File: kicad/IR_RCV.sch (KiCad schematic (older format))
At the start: 19 parts, among them P10 Partition, P5 PR_Host, P6 PR_Slave, P7 Partition, P8 Partition, P9 Partition, Q1 DMN3065LW-7, U6 AD8601

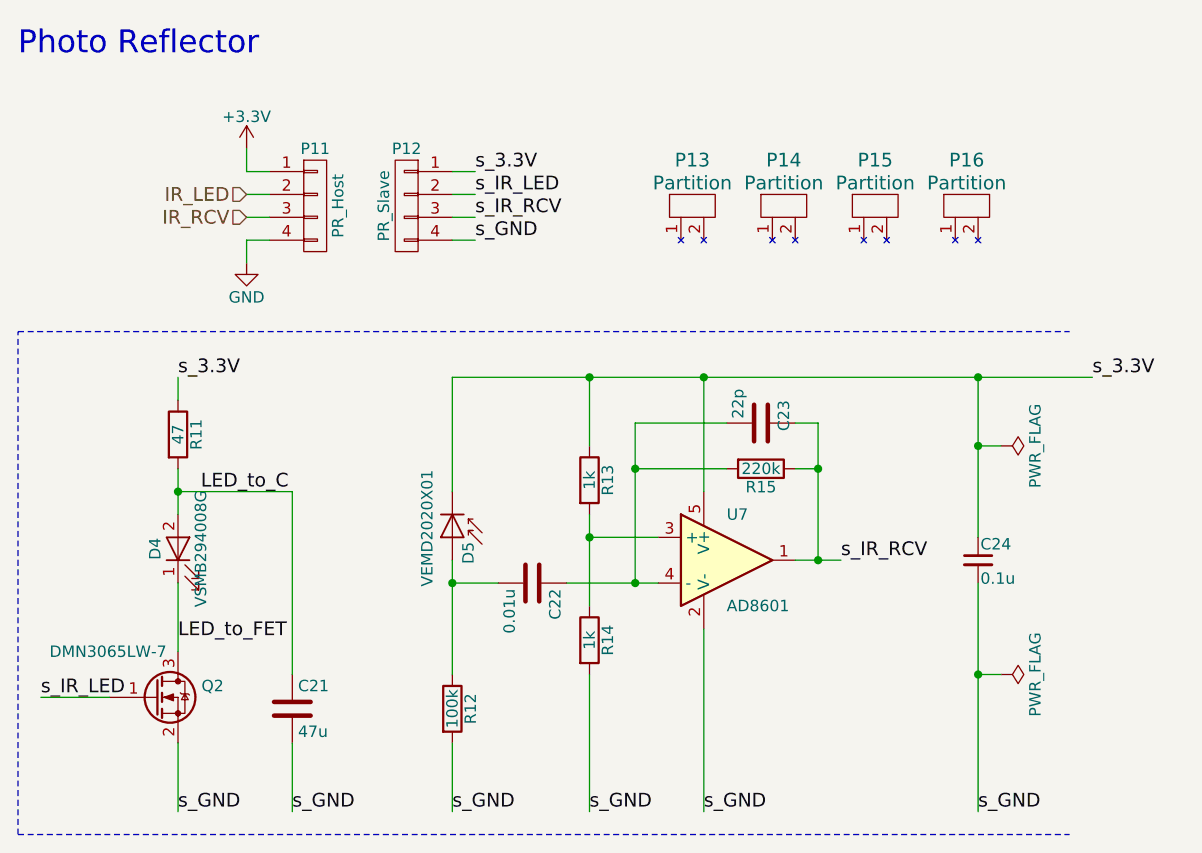
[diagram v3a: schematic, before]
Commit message: フットプリントを改良，アナログ電源を分離
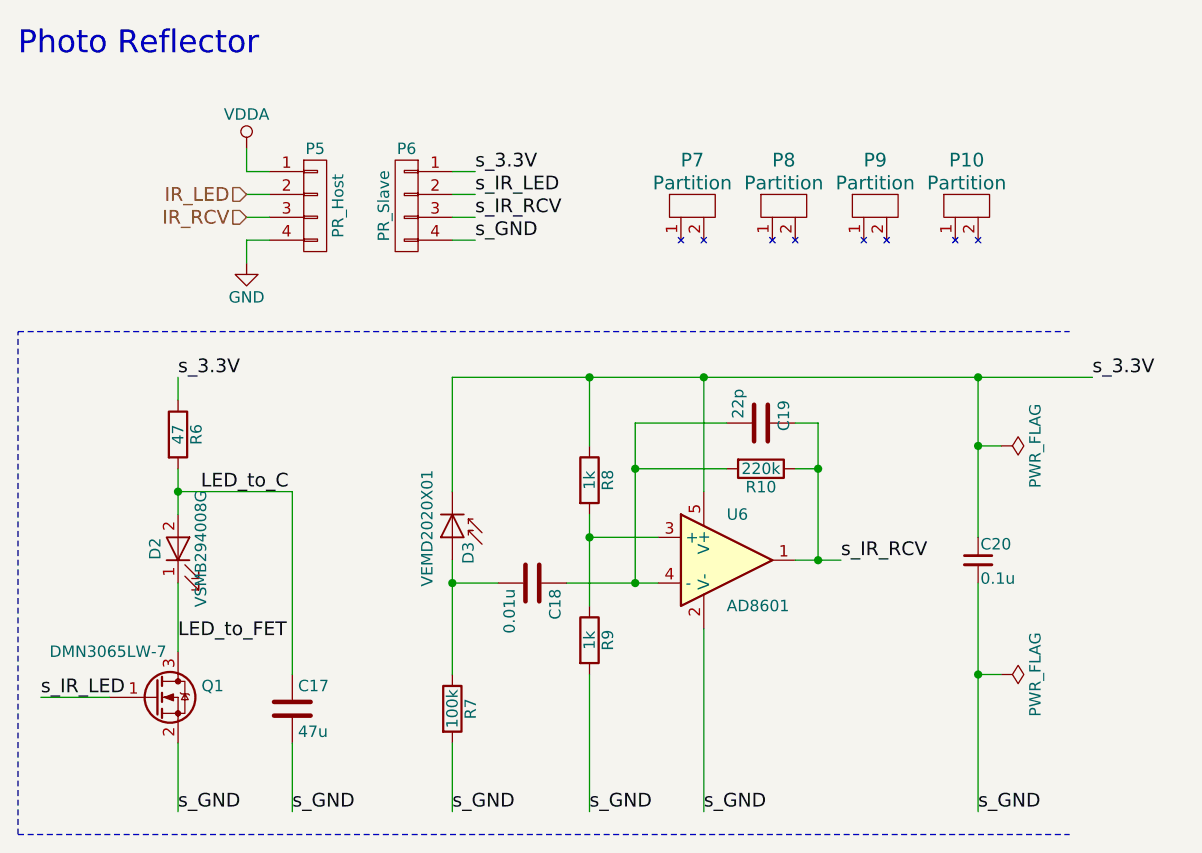
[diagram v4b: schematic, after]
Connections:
- net +3V3 renamed VDDA
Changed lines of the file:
@@
 AR Path="/597E1B35/589BE652" Ref="P25"  Part="1"
 AR Path="/597E1B39/589BE652" Ref="P31"  Part="1"
-F 0 "P12" H 5400 2800 50  0000 C CNN
+F 0 "P6" H 5400 2800 50  0000 C CNN
 F 1 "PR_Slave" V 5500 2550 50  0000 C CNN
 F 2 "mouse:STAND_PR_SLAVE" H 5400 2550 50  0001 C CNN
@@
 AR Path="/597E1B35/589BE75A" Ref="Q5"  Part="1"
 AR Path="/597E1B39/589BE75A" Ref="Q6"  Part="1"
-F 0 "Q2" H 4600 4750 50  0000 R CNN
+F 0 "Q1" H 4600 4750 50  0000 R CNN
 F 1 "DMN3065LW-7" H 4350 4900 50  0000 R CNN
 F 2 "TO_SOT_Packages_SMD:SOT-323_SC-70" H 4500 4800 50  0001 C CNN
@@
 AR Path="/597E1B35/589BE76D" Ref="R24"  Part="1"
 AR Path="/597E1B39/589BE76D" Ref="R29"  Part="1"
-F 0 "R11" V 4480 3550 50  0000 C CNN
+F 0 "R6" V 4480 3550 50  0000 C CNN
 F 1 "47" V 4400 3550 50  0000 C CNN
 F 2 "Resistors_SMD:R_0603" V 4330 3550 50  0001 C CNN
@@
 AR Path="/597E1B35/589BE88F" Ref="P24"  Part="1"
 AR Path="/597E1B39/589BE88F" Ref="P30"  Part="1"
-F 0 "P11" H 5000 2800 50  0000 C CNN
+F 0 "P5" H 5000 2800 50  0000 C CNN
 F 1 "PR_Host" V 5100 2550 50  0000 C CNN
 F 2 "mouse:STAND_PR_HOST" H 5000 2550 50  0001 C CNN
@@
 AR Path="/597E1B35/589BEE3B" Ref="R25"  Part="1"
 AR Path="/597E1B39/589BEE3B" Ref="R30"  Part="1"
-F 0 "R12" V 5680 4750 50  0000 C CNN
+F 0 "R7" V 5680 4750 50  0000 C CNN
 F 1 "100k" V 5600 4750 50  0000 C CNN
 F 2 "Resistors_SMD:R_0201" V 5530 4750 50  0001 C CNN
@@
 AR Path="/597E1B35/589BF265" Ref="#PWR074"  Part="1"
 AR Path="/597E1B39/589BF265" Ref="#PWR078"  Part="1"
-F 0 "#PWR078" H 4700 2550 50  0001 C CNN
+F 0 "#PWR038" H 4700 2550 50  0001 C CNN
 F 1 "GND" H 4700 2650 50  0000 C CNN
 F 2 "" H 4700 2800 50  0000 C CNN
@@
 AR Path="/597E1B35/589EE263" Ref="C32"  Part="1"
 AR Path="/597E1B39/589EE263" Ref="C36"  Part="1"
-F 0 "C21" H 4925 4850 50  0000 L CNN
+F 0 "C17" H 4925 4850 50  0000 L CNN
 F 1 "47u" H 4925 4650 50  0000 L CNN
 F 2 "Capacitors_SMD:C_0805" H 4938 4600 50  0001 C CNN
@@
 Text Label 4500 3800 0    60   ~ 0
 LED_to_C
-$Comp
-L +3.3V #PWR039
-U 1 1 589CC209
-P 4700 2300
-AR Path="/57CF0B09/589CC209" Ref="#PWR039"  Part="1"
-AR Path="/57CF2A30/589CC209" Ref="#PWR043"  Part="1"
-AR Path="/597E1B35/589CC209" Ref="#PWR075"  Part="1"
-AR Path="/597E1B39/589CC209" Ref="#PWR079"  Part="1"
-F 0 "#PWR079" H 4700 2150 50  0001 C CNN
-F 1 "+3.3V" H 4700 2440 50  0000 C CNN
-F 2 "" H 4700 2300 50  0000 C CNN
-F 3 "" H 4700 2300 50  0000 C CNN
-	1    4700 2300
-	1    0    0    -1
-$EndComp
 Text Label 7300 4100 0    60   ~ 0
 s_IR_RCV
@@
 AR Path="/597E1B35/58A0483E" Ref="R26"  Part="1"
 AR Path="/597E1B39/58A0483E" Ref="R31"  Part="1"
-F 0 "R13" V 6280 3750 50  0000 C CNN
+F 0 "R8" V 6280 3750 50  0000 C CNN
 F 1 "1k" V 6200 3750 50  0000 C CNN
 F 2 "Resistors_SMD:R_0201" V 6130 3750 50  0001 C CNN
@@
 AR Path="/597E1B35/57CF0F5E" Ref="C34"  Part="1"
 AR Path="/597E1B39/57CF0F5E" Ref="C38"  Part="1"
-F 0 "C23" H 6850 3600 50  0000 L CNN
+F 0 "C19" H 6850 3600 50  0000 L CNN
 F 1 "22p" H 6800 3400 50  0000 L CNN
 F 2 "Capacitors_SMD:C_0201" H 6988 3350 50  0001 C CNN
@@
 AR Path="/597E1B35/57CF0F57" Ref="R28"  Part="1"
 AR Path="/597E1B39/57CF0F57" Ref="R33"  Part="1"
-F 0 "R15" V 7030 3700 50  0000 C CNN
+F 0 "R10" V 7030 3700 50  0000 C CNN
 F 1 "220k" V 6950 3700 50  0000 C CNN
 F 2 "Resistors_SMD:R_0201" V 6880 3700 50  0001 C CNN
@@
 AR Path="/597E1B35/5925867D" Ref="C35"  Part="1"
 AR Path="/597E1B39/5925867D" Ref="C39"  Part="1"
-F 0 "C24" H 7910 4170 50  0000 L CNN
+F 0 "C20" H 7910 4170 50  0000 L CNN
 F 1 "0.1u" H 7910 4020 50  0000 L CNN
 F 2 "Capacitors_SMD:C_0201" H 7900 4100 50  0001 C CNN
@@
 AR Path="/597E1B35/58A04889" Ref="R27"  Part="1"
 AR Path="/597E1B39/58A04889" Ref="R32"  Part="1"
-F 0 "R14" V 6280 4450 50  0000 C CNN
+F 0 "R9" V 6280 4450 50  0000 C CNN
 F 1 "1k" V 6200 4450 50  0000 C CNN
 F 2 "Resistors_SMD:R_0201" V 6130 4450 50  0001 C CNN
@@
 AR Path="/597E1B35/57CF0F45" Ref="C33"  Part="1"
 AR Path="/597E1B39/57CF0F45" Ref="C37"  Part="1"
-F 0 "C22" H 5975 4300 50  0000 L CNN
+F 0 "C18" H 5975 4300 50  0000 L CNN
 F 1 "0.01u" H 5975 4100 50  0000 L CNN
 F 2 "Capacitors_SMD:C_0201" H 5988 4050 50  0001 C CNN
@@
 AR Path="/597E1B35/59497B18" Ref="P26"  Part="1"
 AR Path="/597E1B39/59497B18" Ref="P32"  Part="1"
-F 0 "P13" H 6650 2550 60  0000 C CNN
+F 0 "P7" H 6650 2550 60  0000 C CNN
 F 1 "Partition" H 6650 2450 60  0000 C CNN
 F 2 "mouse:Partition_Host" H 6650 2450 60  0001 C CNN
@@
 AR Path="/597E1B35/59497CA2" Ref="P27"  Part="1"
 AR Path="/597E1B39/59497CA2" Ref="P33"  Part="1"
-F 0 "P14" H 7050 2550 60  0000 C CNN
+F 0 "P8" H 7050 2550 60  0000 C CNN
 F 1 "Partition" H 7050 2450 60  0000 C CNN
 F 2 "mouse:Partition_Slave" H 7050 2450 60  0001 C CNN
@@
 AR Path="/597E1B35/59497CF1" Ref="P28"  Part="1"
 AR Path="/597E1B39/59497CF1" Ref="P34"  Part="1"
-F 0 "P15" H 7450 2550 60  0000 C CNN
+F 0 "P9" H 7450 2550 60  0000 C CNN
 F 1 "Partition" H 7450 2450 60  0000 C CNN
 F 2 "mouse:Partition_Long_Host" H 7450 2450 60  0001 C CNN
@@
 AR Path="/597E1B35/59497D43" Ref="P29"  Part="1"
 AR Path="/597E1B39/59497D43" Ref="P35"  Part="1"
-F 0 "P16" H 7850 2550 60  0000 C CNN
+F 0 "P10" H 7850 2550 60  0000 C CNN
 F 1 "Partition" H 7850 2450 60  0000 C CNN
 F 2 "mouse:Partition_long_Slave" H 7850 2450 60  0001 C CNN
@@
 AR Path="/597E1B35/594AC13D" Ref="U12"  Part="1"
 AR Path="/597E1B39/594AC13D" Ref="U13"  Part="1"
-F 0 "U7" H 6800 4300 50  0000 L CNN
+F 0 "U6" H 6800 4300 50  0000 L CNN
 F 1 "AD8601" H 6800 3900 50  0000 L CNN
 F 2 "TO_SOT_Packages_SMD:SOT-23-5" H 6800 3700 50  0001 C CNN
@@
 AR Path="/597E1B35/594AC36C" Ref="D11"  Part="1"
 AR Path="/597E1B39/594AC36C" Ref="D13"  Part="1"
-F 0 "D5" H 5620 4070 50  0000 L CNN
+F 0 "D3" H 5620 4070 50  0000 L CNN
 F 1 "VEMD2020X01" H 5560 3890 50  0000 C CNN
 F 2 "mouse:VISHAY_DIODE" H 5550 4000 50  0001 C CNN
@@
 AR Path="/597E1B35/594AC674" Ref="D10"  Part="1"
 AR Path="/597E1B39/594AC674" Ref="D12"  Part="1"
-F 0 "D4" H 4400 4150 50  0000 C CNN
+F 0 "D2" H 4400 4150 50  0000 C CNN
 F 1 "VSMB294008G" H 4400 3950 50  0000 C CNN
 F 2 "mouse:VISHAY_DIODE" H 4400 4050 50  0001 C CNN
@@
 AR Path="/597E1B35/594B7401" Ref="#FLG076"  Part="1"
 AR Path="/597E1B39/594B7401" Ref="#FLG080"  Part="1"
-F 0 "#FLG080" H 8000 3675 50  0001 C CNN
+F 0 "#FLG040" H 8000 3675 50  0001 C CNN
 F 1 "PWR_FLAG" H 8000 3750 50  0000 C CNN
 F 2 "" H 8000 3600 50  0001 C CNN
@@
 AR Path="/597E1B35/594B744C" Ref="#FLG077"  Part="1"
 AR Path="/597E1B39/594B744C" Ref="#FLG081"  Part="1"
-F 0 "#FLG081" H 8000 4675 50  0001 C CNN
+F 0 "#FLG041" H 8000 4675 50  0001 C CNN
 F 1 "PWR_FLAG" H 8000 4750 50  0000 C CNN
 F 2 "" H 8000 4600 50  0001 C CNN
@@
 	7900 3600 8000 3600
 Connection ~ 7900 3600
+$Comp
+L VDDA #PWR?
+U 1 1 59C54857
+P 4700 2300
+F 0 "#PWR?" H 4700 2150 50  0001 C CNN
+F 1 "VDDA" H 4700 2450 50  0000 C CNN
+F 2 "" H 4700 2300 50  0001 C CNN
+F 3 "" H 4700 2300 50  0001 C CNN
+	1    4700 2300
+	1    0    0    -1
+$EndComp
 $EndSCHEMATC

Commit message: 回路とフットプリントを改良
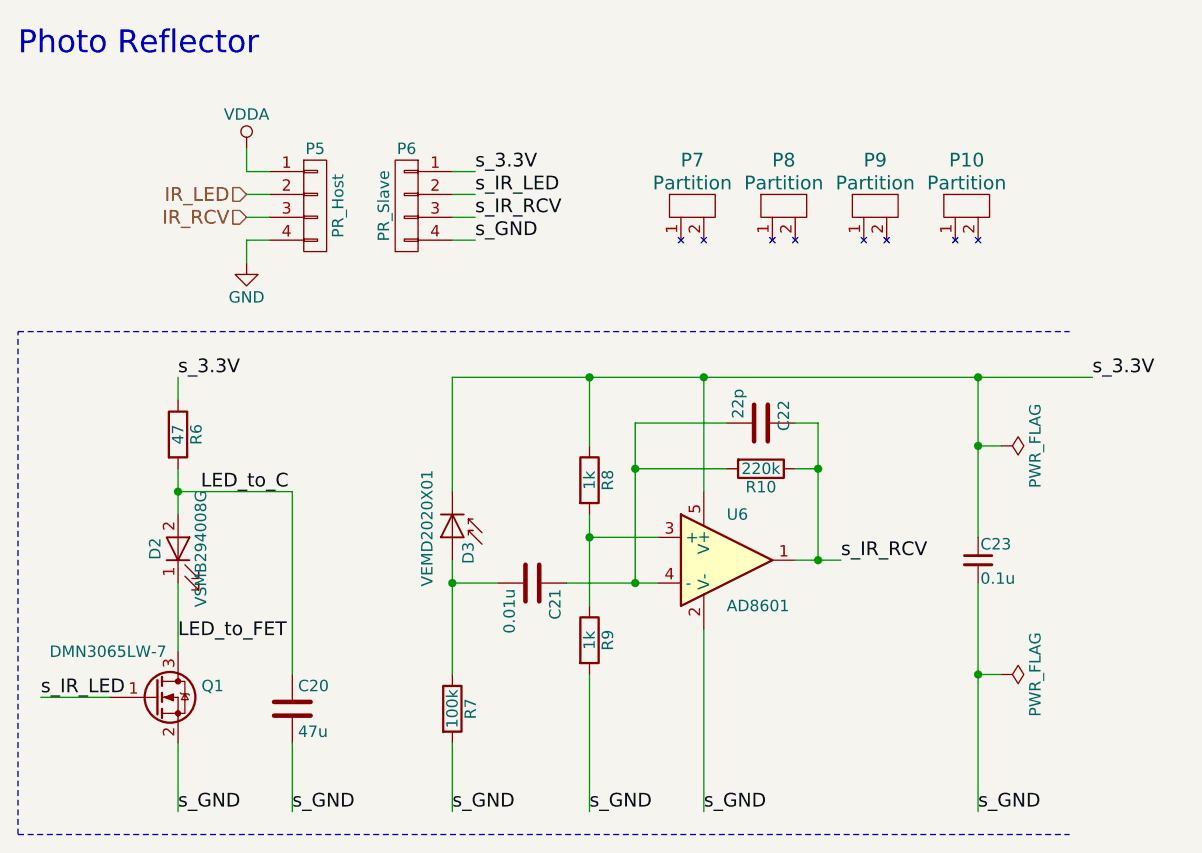
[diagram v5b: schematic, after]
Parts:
- renumbered C17 to C20, C18 to C21, C19 to C22, C20 to C23
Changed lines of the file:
@@
 IR_LED
 $Comp
-L GND #PWR038
+L GND #PWR043
 U 1 1 589BF265
 P 4700 2800
-AR Path="/57CF0B09/589BF265" Ref="#PWR038"  Part="1"
-AR Path="/57CF2A30/589BF265" Ref="#PWR042"  Part="1"
-AR Path="/597E1B35/589BF265" Ref="#PWR074"  Part="1"
-AR Path="/597E1B39/589BF265" Ref="#PWR078"  Part="1"
-F 0 "#PWR038" H 4700 2550 50  0001 C CNN
+AR Path="/57CF0B09/589BF265" Ref="#PWR043"  Part="1"
+AR Path="/57CF2A30/589BF265" Ref="#PWR047"  Part="1"
+AR Path="/597E1B35/589BF265" Ref="#PWR079"  Part="1"
+AR Path="/597E1B39/589BF265" Ref="#PWR083"  Part="1"
+F 0 "#PWR083" H 4700 2550 50  0001 C CNN
 F 1 "GND" H 4700 2650 50  0000 C CNN
 F 2 "" H 4700 2800 50  0000 C CNN
@@
 s_3.3V
 $Comp
-L C C17
+L C C20
 U 1 1 589EE263
 P 4900 4750
-AR Path="/57CF0B09/589EE263" Ref="C17"  Part="1"
-AR Path="/57CF2A30/589EE263" Ref="C21"  Part="1"
-AR Path="/597E1B35/589EE263" Ref="C32"  Part="1"
-AR Path="/597E1B39/589EE263" Ref="C36"  Part="1"
-F 0 "C17" H 4925 4850 50  0000 L CNN
+AR Path="/57CF0B09/589EE263" Ref="C20"  Part="1"
+AR Path="/57CF2A30/589EE263" Ref="C24"  Part="1"
+AR Path="/597E1B35/589EE263" Ref="C34"  Part="1"
+AR Path="/597E1B39/589EE263" Ref="C38"  Part="1"
+F 0 "C20" H 4925 4850 50  0000 L CNN
 F 1 "47u" H 4925 4650 50  0000 L CNN
 F 2 "Capacitors_SMD:C_0805" H 4938 4600 50  0001 C CNN
@@
 s_3.3V
 $Comp
-L C C19
+L C C22
 U 1 1 57CF0F5E
 P 6950 3500
-AR Path="/57CF0B09/57CF0F5E" Ref="C19"  Part="1"
-AR Path="/57CF2A30/57CF0F5E" Ref="C23"  Part="1"
-AR Path="/597E1B35/57CF0F5E" Ref="C34"  Part="1"
-AR Path="/597E1B39/57CF0F5E" Ref="C38"  Part="1"
-F 0 "C19" H 6850 3600 50  0000 L CNN
+AR Path="/57CF0B09/57CF0F5E" Ref="C22"  Part="1"
+AR Path="/57CF2A30/57CF0F5E" Ref="C26"  Part="1"
+AR Path="/597E1B35/57CF0F5E" Ref="C36"  Part="1"
+AR Path="/597E1B39/57CF0F5E" Ref="C40"  Part="1"
+F 0 "C22" H 6850 3600 50  0000 L CNN
 F 1 "22p" H 6800 3400 50  0000 L CNN
 F 2 "Capacitors_SMD:C_0201" H 6988 3350 50  0001 C CNN
@@
 s_GND
 $Comp
-L C_Small C20
+L C_Small C23
 U 1 1 5925867D
 P 7900 4100
-AR Path="/57CF0B09/5925867D" Ref="C20"  Part="1"
-AR Path="/57CF2A30/5925867D" Ref="C24"  Part="1"
-AR Path="/597E1B35/5925867D" Ref="C35"  Part="1"
-AR Path="/597E1B39/5925867D" Ref="C39"  Part="1"
-F 0 "C20" H 7910 4170 50  0000 L CNN
+AR Path="/57CF0B09/5925867D" Ref="C23"  Part="1"
+AR Path="/57CF2A30/5925867D" Ref="C27"  Part="1"
+AR Path="/597E1B35/5925867D" Ref="C37"  Part="1"
+AR Path="/597E1B39/5925867D" Ref="C41"  Part="1"
+F 0 "C23" H 7910 4170 50  0000 L CNN
 F 1 "0.1u" H 7910 4020 50  0000 L CNN
 F 2 "Capacitors_SMD:C_0201" H 7900 4100 50  0001 C CNN
@@
 	6100 4200 6500 4200
 $Comp
-L C C18
+L C C21
 U 1 1 57CF0F45
 P 5950 4200
-AR Path="/57CF0B09/57CF0F45" Ref="C18"  Part="1"
-AR Path="/57CF2A30/57CF0F45" Ref="C22"  Part="1"
-AR Path="/597E1B35/57CF0F45" Ref="C33"  Part="1"
-AR Path="/597E1B39/57CF0F45" Ref="C37"  Part="1"
-F 0 "C18" H 5975 4300 50  0000 L CNN
+AR Path="/57CF0B09/57CF0F45" Ref="C21"  Part="1"
+AR Path="/57CF2A30/57CF0F45" Ref="C25"  Part="1"
+AR Path="/597E1B35/57CF0F45" Ref="C35"  Part="1"
+AR Path="/597E1B39/57CF0F45" Ref="C39"  Part="1"
+F 0 "C21" H 5975 4300 50  0000 L CNN
 F 1 "0.01u" H 5975 4100 50  0000 L CNN
 F 2 "Capacitors_SMD:C_0201" H 5988 4050 50  0001 C CNN
@@
 $EndComp
 $Comp
-L PWR_FLAG #FLG040
+L PWR_FLAG #FLG044
 U 1 1 594B7401
 P 8000 3600
-AR Path="/57CF0B09/594B7401" Ref="#FLG040"  Part="1"
-AR Path="/57CF2A30/594B7401" Ref="#FLG044"  Part="1"
-AR Path="/597E1B35/594B7401" Ref="#FLG076"  Part="1"
-AR Path="/597E1B39/594B7401" Ref="#FLG080"  Part="1"
-F 0 "#FLG040" H 8000 3675 50  0001 C CNN
+AR Path="/57CF0B09/594B7401" Ref="#FLG044"  Part="1"
+AR Path="/57CF2A30/594B7401" Ref="#FLG048"  Part="1"
+AR Path="/597E1B35/594B7401" Ref="#FLG080"  Part="1"
+AR Path="/597E1B39/594B7401" Ref="#FLG084"  Part="1"
+F 0 "#FLG084" H 8000 3675 50  0001 C CNN
 F 1 "PWR_FLAG" H 8000 3750 50  0000 C CNN
 F 2 "" H 8000 3600 50  0001 C CNN
@@
 $EndComp
 $Comp
-L PWR_FLAG #FLG041
+L PWR_FLAG #FLG045
 U 1 1 594B744C
 P 8000 4600
-AR Path="/57CF0B09/594B744C" Ref="#FLG041"  Part="1"
-AR Path="/57CF2A30/594B744C" Ref="#FLG045"  Part="1"
-AR Path="/597E1B35/594B744C" Ref="#FLG077"  Part="1"
-AR Path="/597E1B39/594B744C" Ref="#FLG081"  Part="1"
-F 0 "#FLG041" H 8000 4675 50  0001 C CNN
+AR Path="/57CF0B09/594B744C" Ref="#FLG045"  Part="1"
+AR Path="/57CF2A30/594B744C" Ref="#FLG049"  Part="1"
+AR Path="/597E1B35/594B744C" Ref="#FLG081"  Part="1"
+AR Path="/597E1B39/594B744C" Ref="#FLG085"  Part="1"
+F 0 "#FLG085" H 8000 4675 50  0001 C CNN
 F 1 "PWR_FLAG" H 8000 4750 50  0000 C CNN
 F 2 "" H 8000 4600 50  0001 C CNN
@@
 Connection ~ 7900 3600
 $Comp
-L VDDA #PWR?
+L VDDA #PWR046
 U 1 1 59C54857
 P 4700 2300
-F 0 "#PWR?" H 4700 2150 50  0001 C CNN
+AR Path="/57CF0B09/59C54857" Ref="#PWR046"  Part="1"
+AR Path="/57CF2A30/59C54857" Ref="#PWR050"  Part="1"
+AR Path="/597E1B35/59C54857" Ref="#PWR082"  Part="1"
+AR Path="/597E1B39/59C54857" Ref="#PWR086"  Part="1"
+F 0 "#PWR086" H 4700 2150 50  0001 C CNN
 F 1 "VDDA" H 4700 2450 50  0000 C CNN
 F 2 "" H 4700 2300 50  0001 C CNN

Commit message: 自動配線1残し
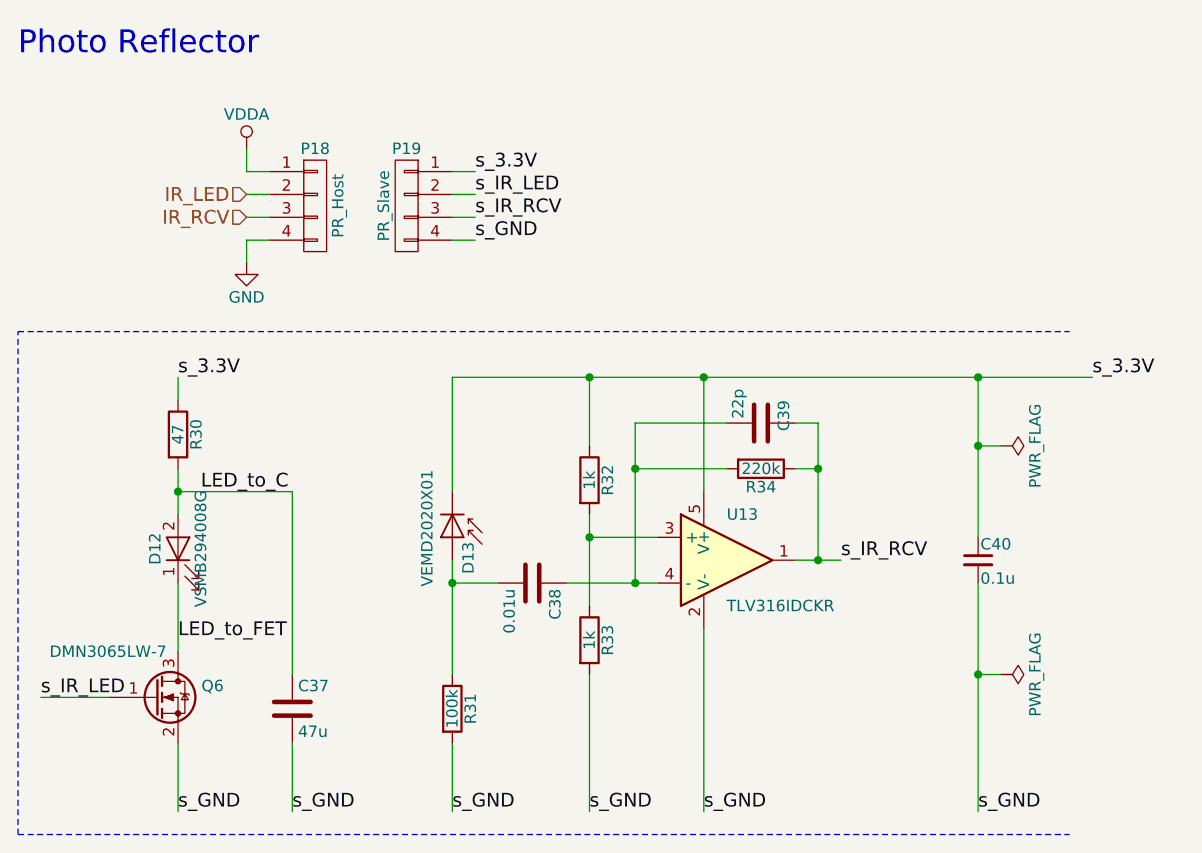
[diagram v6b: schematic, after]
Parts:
- removed P10: Partition, mouse:Partition_long_Slave, symbol Partition
- removed P7: Partition, mouse:Partition_Host, symbol Partition
- removed P8: Partition, mouse:Partition_Slave, symbol Partition
- removed P9: Partition, mouse:Partition_Long_Host, symbol Partition
- U6: value AD8601 -> TLV316IDCKR; footprint TO_SOT_Packages_SMD:SOT-23-5 -> TO_SOT_Packages_SMD:SOT-353_SC-70-5
- renumbered C20 to C19, C21 to C20, C22 to C21, C23 to C22
